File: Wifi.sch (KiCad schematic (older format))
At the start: 15 parts

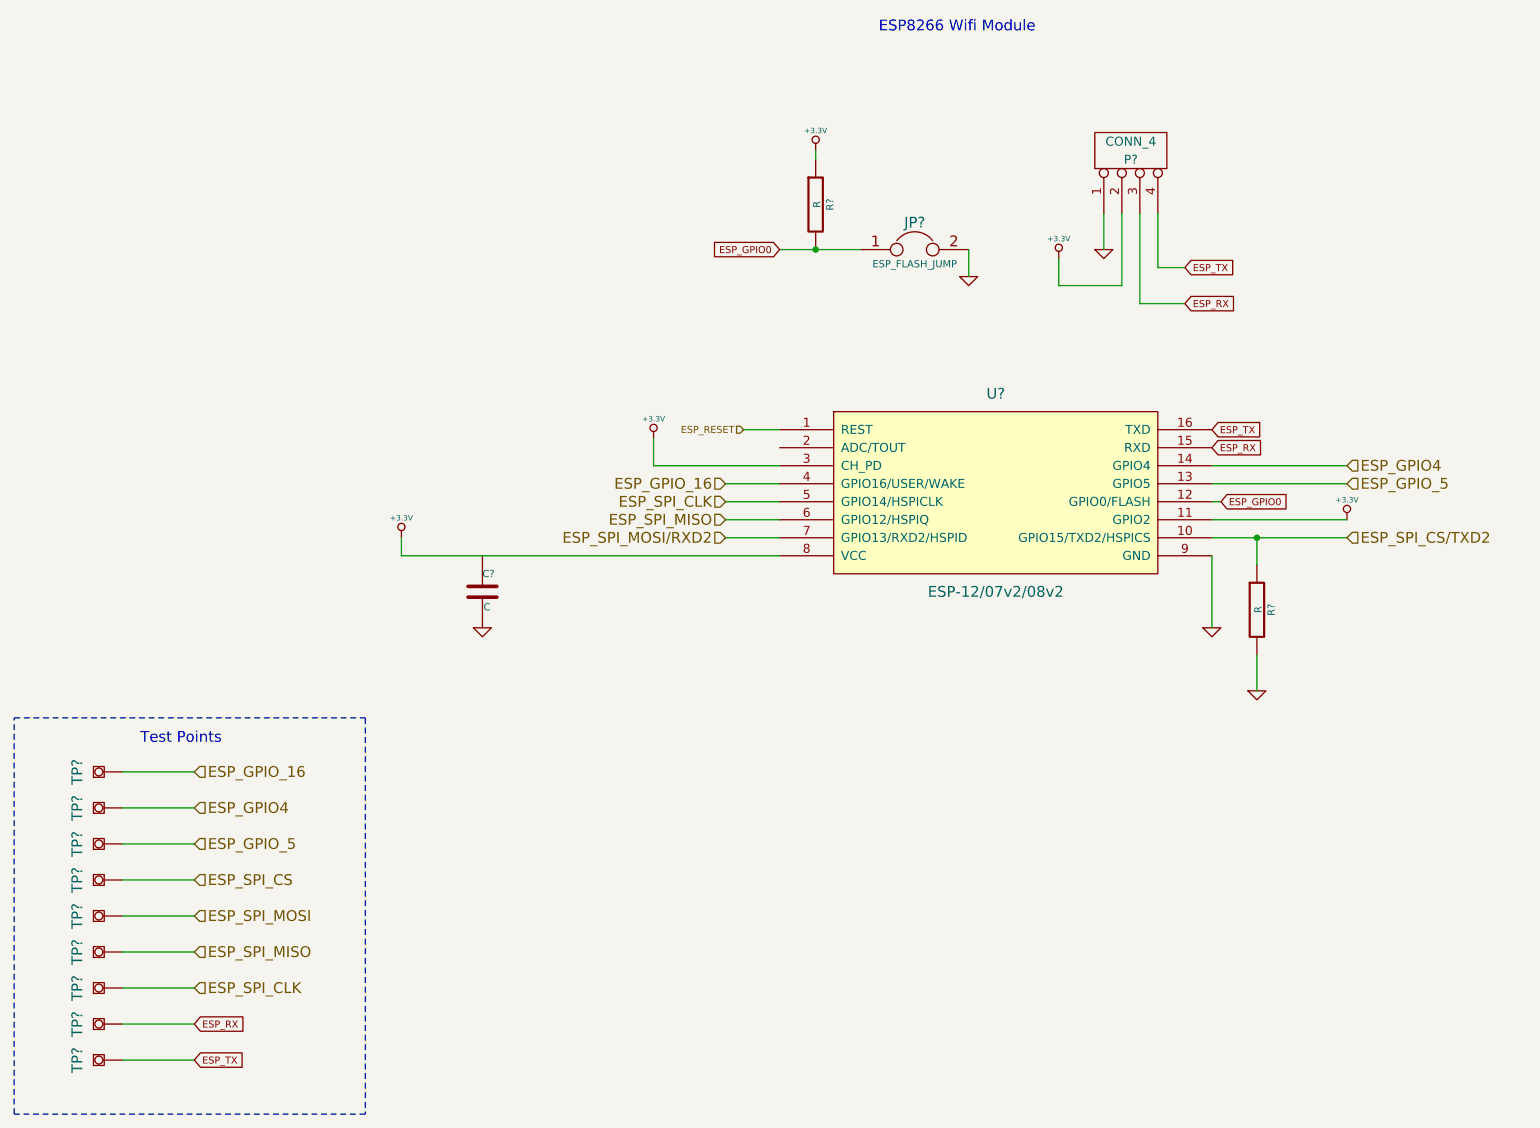
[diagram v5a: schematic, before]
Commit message: ESP doesn't seem to support UART2, switch to UART1
As far as I can tell the TXD2, RXD2 ports are not documented
If they do work, they will only work exclusively of TX1/RX1.
So better to just use the main UART.
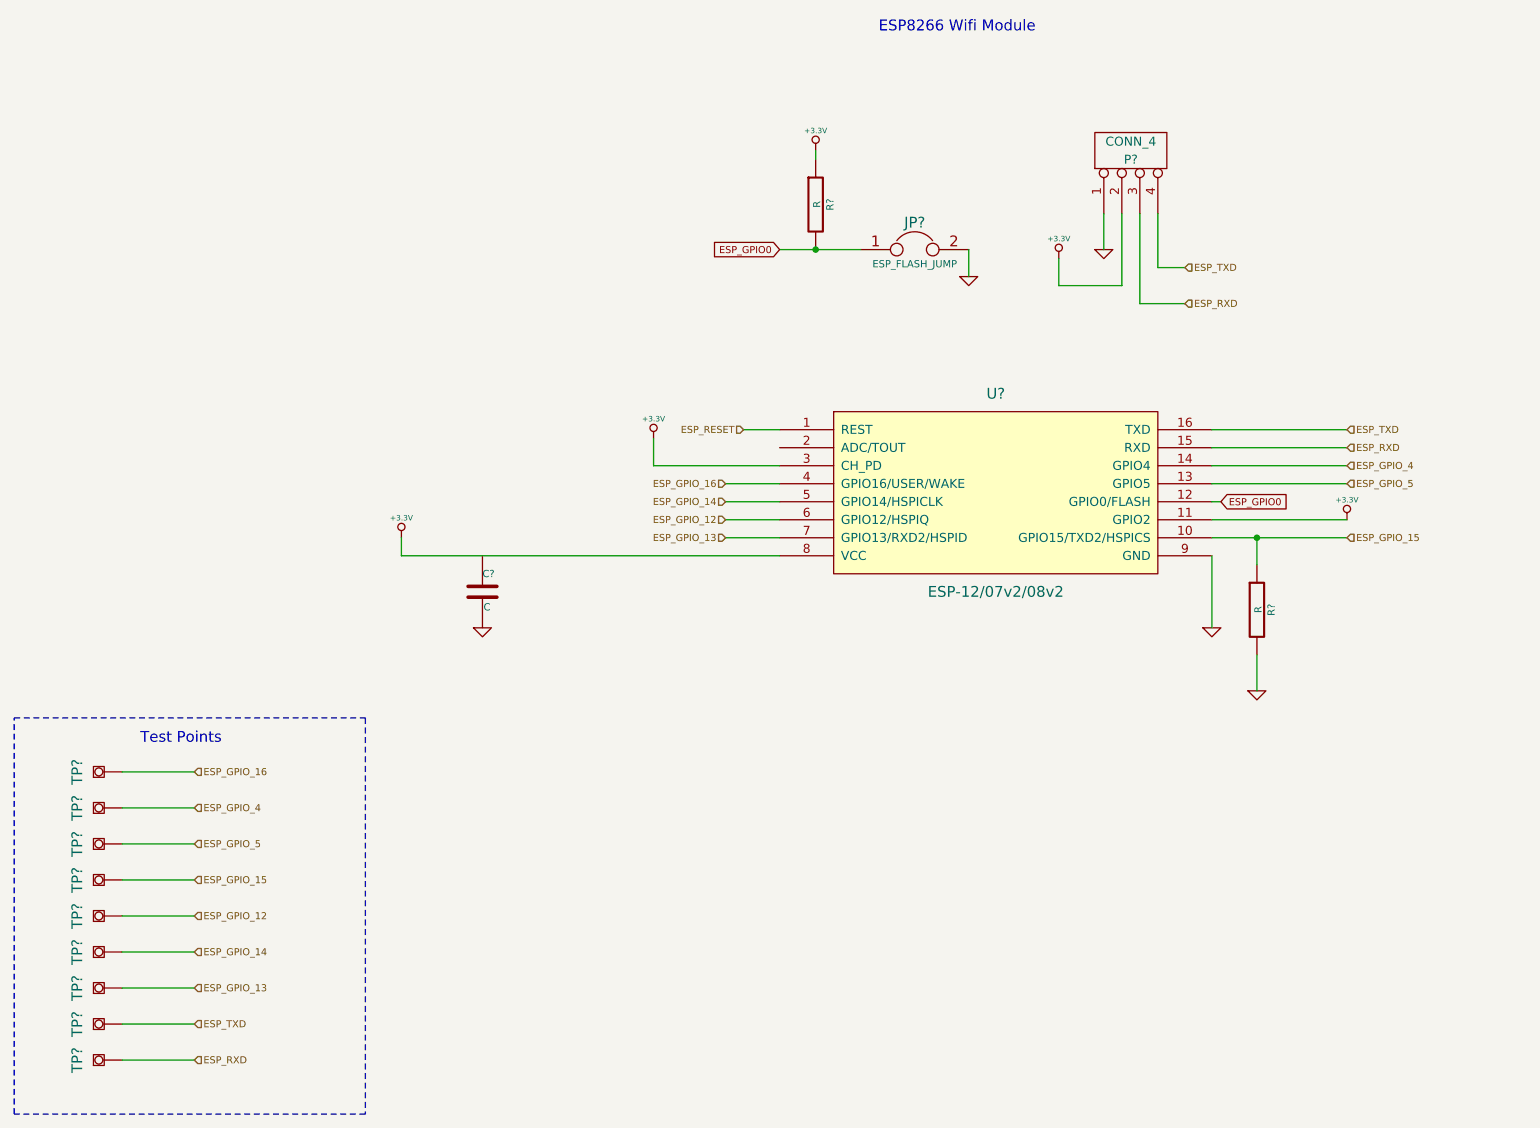
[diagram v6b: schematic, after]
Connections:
- net ESP_SPI_CS/TXD2 is gone; now on net ESP_GPIO_15: R?.1, U?.10 (GPIO15/TXD2/HSPICS)
- net ESP_SPI_MOSI is gone; now on net ESP_GPIO_12: TP?.1
- net ESP_SPI_MOSI/RXD2 is gone; now on net ESP_GPIO_13: U?.7 (GPIO13/RXD2/HSPID)
- net ESP_GPIO4 renamed ESP_GPIO_4
- net ESP_RX renamed ESP_RXD
- net ESP_RXD: now also TP?.1; no longer TP?.1
- net ESP_SPI_CLK renamed ESP_GPIO_13
- net ESP_GPIO_13: no longer U?.5 (GPIO14/HSPICLK)
- net ESP_SPI_CS renamed ESP_GPIO_15
- net ESP_SPI_MISO renamed ESP_GPIO_12
- net ESP_GPIO_12: no longer TP?.1
- net ESP_TX renamed ESP_TXD
- net ESP_TXD: now also TP?.1; no longer TP?.1
- new net ESP_GPIO_14: TP?.1, U?.5 (GPIO14/HSPICLK)
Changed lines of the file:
@@
 	1    0    0    -1
 $EndComp
-Text GLabel 7100 3200 2    39   Input ~ 0
-ESP_RX
-Text GLabel 7100 3000 2    39   Input ~ 0
-ESP_TX
 $Comp
 L JUMPER JP?
@@
 	1    0    0    -1
 $EndComp
-Text GLabel 7250 4000 2    39   Input ~ 0
-ESP_RX
-Text GLabel 1600 7400 2    39   Input ~ 0
-ESP_TX
-Text HLabel 4550 4300 0    60   Input ~ 0
-ESP_SPI_CLK
-Text HLabel 4550 4400 0    60   Input ~ 0
-ESP_SPI_MISO
-Text HLabel 4550 4500 0    60   Input ~ 0
-ESP_SPI_MOSI/RXD2
 $Comp
 L R R?
@@
 	1    0    0    -1
 $EndComp
-Text HLabel 8000 4500 2    60   Input ~ 0
-ESP_SPI_CS/TXD2
 $Comp
 L +3.3V #PWR?
@@
 Text GLabel 7300 4300 2    39   Input ~ 0
 ESP_GPIO0
-Text HLabel 8000 4100 2    60   Input ~ 0
-ESP_GPIO4
-Text HLabel 8000 4200 2    60   Input ~ 0
+Text HLabel 8000 4100 2    39   Input ~ 0
+ESP_GPIO_4
+Text HLabel 8000 4200 2    39   Input ~ 0
 ESP_GPIO_5
-Text HLabel 4550 4200 0    60   Input ~ 0
+Text HLabel 4550 4200 0    39   Input ~ 0
 ESP_GPIO_16
 $Comp
@@
 Wire Wire Line
 	1200 7000 1600 7000
-Text HLabel 1600 5800 2    60   Input ~ 0
+Text HLabel 1600 5800 2    39   Input ~ 0
 ESP_GPIO_16
-Text HLabel 1600 7000 2    60   Input ~ 0
-ESP_SPI_CLK
-Text HLabel 1600 6800 2    60   Input ~ 0
-ESP_SPI_MISO
-Text HLabel 1600 6600 2    60   Input ~ 0
-ESP_SPI_MOSI
-Text HLabel 1600 6400 2    60   Input ~ 0
-ESP_SPI_CS
-Text HLabel 1600 6200 2    60   Input ~ 0
+Text HLabel 1600 6200 2    39   Input ~ 0
 ESP_GPIO_5
-Text HLabel 1600 6000 2    60   Input ~ 0
-ESP_GPIO4
+Text HLabel 1600 6000 2    39   Input ~ 0
+ESP_GPIO_4
 $Comp
 L TESTPOINT TP?
@@
 Wire Wire Line
 	1200 7400 1600 7400
-Text GLabel 1600 7200 2    39   Input ~ 0
-ESP_RX
-Text GLabel 7250 3900 2    39   Input ~ 0
-ESP_TX
 Wire Notes Line
 	600  5500 2550 5500
@@
 Text HLabel 4650 3900 0    39   Input ~ 0
 ESP_RESET
+Text HLabel 8000 3900 2    39   Input ~ 0
+ESP_TXD
+Text HLabel 8000 4000 2    39   Input ~ 0
+ESP_RXD
+Text HLabel 7100 3200 2    39   Input ~ 0
+ESP_RXD
+Text HLabel 7100 3000 2    39   Input ~ 0
+ESP_TXD
+Wire Wire Line
+	8000 4000 7250 4000
+Wire Wire Line
+	7250 3900 8000 3900
+Text HLabel 1600 7200 2    39   Input ~ 0
+ESP_TXD
+Text HLabel 1600 7400 2    39   Input ~ 0
+ESP_RXD
+Text HLabel 4550 4300 0    39   Input ~ 0
+ESP_GPIO_14
+Text HLabel 4550 4400 0    39   Input ~ 0
+ESP_GPIO_12
+Text HLabel 4550 4500 0    39   Input ~ 0
+ESP_GPIO_13
+Text HLabel 8000 4500 2    39   Input ~ 0
+ESP_GPIO_15
+Text HLabel 1600 6400 2    39   Input ~ 0
+ESP_GPIO_15
+Text HLabel 1600 6600 2    39   Input ~ 0
+ESP_GPIO_12
+Text HLabel 1600 6800 2    39   Input ~ 0
+ESP_GPIO_14
+Text HLabel 1600 7000 2    39   Input ~ 0
+ESP_GPIO_13
 $EndSCHEMATC

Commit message: Think sch finished
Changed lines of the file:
@@
 $EndComp
 $Comp
-L GND #PWR?
+L GND #PWR054
 U 1 1 55667722
 P 6650 2900
-F 0 "#PWR?" H 6650 2900 30  0001 C CNN
+F 0 "#PWR054" H 6650 2900 30  0001 C CNN
 F 1 "GND" H 6650 2830 30  0001 C CNN
 F 2 "" H 6650 2900 60  0000 C CNN
@@
 $EndComp
 $Comp
-L +3.3V #PWR?
+L +3.3V #PWR055
 U 1 1 55667729
 P 6400 2950
-F 0 "#PWR?" H 6400 2910 30  0001 C CNN
+F 0 "#PWR055" H 6400 2910 30  0001 C CNN
 F 1 "+3.3V" H 6400 3060 30  0000 C CNN
 F 2 "" H 6400 2950 60  0000 C CNN
@@
 $EndComp
 $Comp
-L +3.3V #PWR?
+L +3.3V #PWR056
 U 1 1 55667746
 P 5050 2350
-F 0 "#PWR?" H 5050 2310 30  0001 C CNN
+F 0 "#PWR056" H 5050 2310 30  0001 C CNN
 F 1 "+3.3V" H 5050 2460 30  0000 C CNN
 F 2 "" H 5050 2350 60  0000 C CNN
@@
 $EndComp
 $Comp
-L GND #PWR?
+L GND #PWR057
 U 1 1 5566774C
 P 5900 3050
-F 0 "#PWR?" H 5900 3050 30  0001 C CNN
+F 0 "#PWR057" H 5900 3050 30  0001 C CNN
 F 1 "GND" H 5900 2980 30  0001 C CNN
 F 2 "" H 5900 3050 60  0000 C CNN
@@
 ESP8266 Wifi Module
 $Comp
-L +3.3V #PWR?
+L +3.3V #PWR058
 U 1 1 5566775A
 P 8000 4400
-F 0 "#PWR?" H 8000 4360 30  0001 C CNN
+F 0 "#PWR058" H 8000 4360 30  0001 C CNN
 F 1 "+3.3V" H 8000 4510 30  0000 C CNN
 F 2 "" H 8000 4400 60  0000 C CNN
@@
 $EndComp
 $Comp
-L +3.3V #PWR?
+L +3.3V #PWR059
 U 1 1 55667760
 P 4150 3950
-F 0 "#PWR?" H 4150 3910 30  0001 C CNN
+F 0 "#PWR059" H 4150 3910 30  0001 C CNN
 F 1 "+3.3V" H 4150 4060 30  0000 C CNN
 F 2 "" H 4150 3950 60  0000 C CNN
@@
 $EndComp
 $Comp
-L GND #PWR?
+L GND #PWR060
 U 1 1 5566776E
 P 7500 5350
-F 0 "#PWR?" H 7500 5350 30  0001 C CNN
+F 0 "#PWR060" H 7500 5350 30  0001 C CNN
 F 1 "GND" H 7500 5280 30  0001 C CNN
 F 2 "" H 7500 5350 60  0000 C CNN
@@
 $EndComp
 $Comp
-L +3.3V #PWR?
+L +3.3V #PWR061
 U 1 1 5566915C
 P 2750 4500
-F 0 "#PWR?" H 2750 4460 30  0001 C CNN
+F 0 "#PWR061" H 2750 4460 30  0001 C CNN
 F 1 "+3.3V" H 2750 4610 30  0000 C CNN
 F 2 "" H 2750 4500 60  0000 C CNN
@@
 $EndComp
 $Comp
-L GND #PWR?
+L GND #PWR062
 U 1 1 556691BF
 P 7250 5000
-F 0 "#PWR?" H 7250 5000 30  0001 C CNN
+F 0 "#PWR062" H 7250 5000 30  0001 C CNN
 F 1 "GND" H 7250 4930 30  0001 C CNN
 F 2 "" H 7250 5000 60  0000 C CNN
@@
 $EndComp
 $Comp
-L GND #PWR?
+L GND #PWR063
 U 1 1 5566925F
 P 3200 5000
-F 0 "#PWR?" H 3200 5000 30  0001 C CNN
+F 0 "#PWR063" H 3200 5000 30  0001 C CNN
 F 1 "GND" H 3200 4930 30  0001 C CNN
 F 2 "" H 3200 5000 60  0000 C CNN
@@
 	5050 2350 5050 2400
 Wire Wire Line
-	4850 2900 5300 2900
+	4850 2900 5050 2900
+Wire Wire Line
+	5050 2900 5300 2900
 Wire Wire Line
 	5900 2900 5900 3050
@@
 	7250 4300 7300 4300
 Wire Wire Line
-	7250 4500 8000 4500
+	7250 4500 7500 4500
+Wire Wire Line
+	7500 4500 8000 4500
 Wire Wire Line
 	7500 4500 7500 4650
@@
 Text HLabel 7100 3000 2    39   Input ~ 0
 ESP_TXD
-Wire Wire Line
-	8000 4000 7250 4000
-Wire Wire Line
-	7250 3900 8000 3900
 Text HLabel 1600 7200 2    39   Input ~ 0
 ESP_TXD
@@
 Text HLabel 1600 7000 2    39   Input ~ 0
 ESP_GPIO_13
+Wire Wire Line
+	7250 3900 7950 3900
+Wire Wire Line
+	7950 3900 8000 3900
+Wire Wire Line
+	7250 4000 7650 4000
+Wire Wire Line
+	7650 4000 8000 4000
 $EndSCHEMATC

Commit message: DRCs mostly fixed
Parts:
- gave numbers to parts that had none: 15
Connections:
- net +3.3V: now also C12.1
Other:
- moved on the sheet: C12
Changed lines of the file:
@@
 $EndDescr
 $Comp
-L ESP-12/07v2/08v2 U?
+L ESP-12/07v2/08v2 U8
 U 1 1 55667714
 P 6050 4250
-F 0 "U?" H 6050 4800 60  0000 C CNN
+F 0 "U8" H 6050 4800 60  0000 C CNN
 F 1 "ESP-12/07v2/08v2" H 6050 3700 60  0000 C CNN
 F 2 "" H 6050 4250 60  0000 C CNN
@@
 $EndComp
 $Comp
-L CONN_4 P?
+L CONN_4 P5
 U 1 1 5566771B
 P 6800 2350
-F 0 "P?" V 6750 2350 50  0000 C CNN
+F 0 "P5" V 6750 2350 50  0000 C CNN
 F 1 "CONN_4" V 6850 2350 50  0000 C CNN
 F 2 "" H 6800 2350 60  0000 C CNN
@@
 $EndComp
 $Comp
-L GND #PWR054
+L GND #PWR056
 U 1 1 55667722
 P 6650 2900
-F 0 "#PWR054" H 6650 2900 30  0001 C CNN
+F 0 "#PWR056" H 6650 2900 30  0001 C CNN
 F 1 "GND" H 6650 2830 30  0001 C CNN
 F 2 "" H 6650 2900 60  0000 C CNN
@@
 $EndComp
 $Comp
-L +3.3V #PWR055
+L +3.3V #PWR057
 U 1 1 55667729
 P 6400 2950
-F 0 "#PWR055" H 6400 2910 30  0001 C CNN
+F 0 "#PWR057" H 6400 2910 30  0001 C CNN
 F 1 "+3.3V" H 6400 3060 30  0000 C CNN
 F 2 "" H 6400 2950 60  0000 C CNN
@@
 $EndComp
 $Comp
-L JUMPER JP?
+L JUMPER JP2
 U 1 1 55667738
 P 5600 2900
-F 0 "JP?" H 5600 3050 60  0000 C CNN
+F 0 "JP2" H 5600 3050 60  0000 C CNN
 F 1 "ESP_FLASH_JUMP" H 5600 2820 40  0000 C CNN
 F 2 "" H 5600 2900 60  0000 C CNN
@@
 $EndComp
 $Comp
-L R R?
+L R R10
 U 1 1 5566773F
 P 5050 2650
-F 0 "R?" V 5130 2650 40  0000 C CNN
+F 0 "R10" V 5130 2650 40  0000 C CNN
 F 1 "R" V 5057 2651 40  0000 C CNN
 F 2 "" V 4980 2650 30  0000 C CNN
@@
 $EndComp
 $Comp
-L +3.3V #PWR056
+L +3.3V #PWR058
 U 1 1 55667746
 P 5050 2350
-F 0 "#PWR056" H 5050 2310 30  0001 C CNN
+F 0 "#PWR058" H 5050 2310 30  0001 C CNN
 F 1 "+3.3V" H 5050 2460 30  0000 C CNN
 F 2 "" H 5050 2350 60  0000 C CNN
@@
 $EndComp
 $Comp
-L GND #PWR057
+L GND #PWR059
 U 1 1 5566774C
 P 5900 3050
-F 0 "#PWR057" H 5900 3050 30  0001 C CNN
+F 0 "#PWR059" H 5900 3050 30  0001 C CNN
 F 1 "GND" H 5900 2980 30  0001 C CNN
 F 2 "" H 5900 3050 60  0000 C CNN
@@
 ESP8266 Wifi Module
 $Comp
-L +3.3V #PWR058
+L +3.3V #PWR060
 U 1 1 5566775A
 P 8000 4400
-F 0 "#PWR058" H 8000 4360 30  0001 C CNN
+F 0 "#PWR060" H 8000 4360 30  0001 C CNN
 F 1 "+3.3V" H 8000 4510 30  0000 C CNN
 F 2 "" H 8000 4400 60  0000 C CNN
@@
 $EndComp
 $Comp
-L +3.3V #PWR059
+L +3.3V #PWR061
 U 1 1 55667760
 P 4150 3950
-F 0 "#PWR059" H 4150 3910 30  0001 C CNN
+F 0 "#PWR061" H 4150 3910 30  0001 C CNN
 F 1 "+3.3V" H 4150 4060 30  0000 C CNN
 F 2 "" H 4150 3950 60  0000 C CNN
@@
 $EndComp
 $Comp
-L GND #PWR060
+L GND #PWR062
 U 1 1 5566776E
 P 7500 5350
-F 0 "#PWR060" H 7500 5350 30  0001 C CNN
+F 0 "#PWR062" H 7500 5350 30  0001 C CNN
 F 1 "GND" H 7500 5280 30  0001 C CNN
 F 2 "" H 7500 5350 60  0000 C CNN
@@
 $EndComp
 $Comp
-L R R?
+L R R11
 U 1 1 55668FA2
 P 7500 4900
-F 0 "R?" V 7580 4900 40  0000 C CNN
+F 0 "R11" V 7580 4900 40  0000 C CNN
 F 1 "R" V 7507 4901 40  0000 C CNN
 F 2 "" V 7430 4900 30  0000 C CNN
@@
 $EndComp
 $Comp
-L +3.3V #PWR061
+L +3.3V #PWR063
 U 1 1 5566915C
 P 2750 4500
-F 0 "#PWR061" H 2750 4460 30  0001 C CNN
+F 0 "#PWR063" H 2750 4460 30  0001 C CNN
 F 1 "+3.3V" H 2750 4610 30  0000 C CNN
 F 2 "" H 2750 4500 60  0000 C CNN
@@
 $EndComp
 $Comp
-L GND #PWR062
+L GND #PWR064
 U 1 1 556691BF
 P 7250 5000
-F 0 "#PWR062" H 7250 5000 30  0001 C CNN
+F 0 "#PWR064" H 7250 5000 30  0001 C CNN
 F 1 "GND" H 7250 4930 30  0001 C CNN
 F 2 "" H 7250 5000 60  0000 C CNN
@@
 $EndComp
 $Comp
-L C C?
+L C C12
 U 1 1 5566923C
-P 3200 4800
-F 0 "C?" H 3200 4900 40  0000 L CNN
-F 1 "C" H 3206 4715 40  0000 L CNN
-F 2 "" H 3238 4650 30  0000 C CNN
-F 3 "" H 3200 4800 60  0000 C CNN
-	1    3200 4800
-	1    0    0    -1
-$EndComp
-$Comp
-L GND #PWR063
+P 3450 4850
+F 0 "C12" H 3450 4950 40  0000 L CNN
+F 1 "C" H 3456 4765 40  0000 L CNN
+F 2 "" H 3488 4700 30  0000 C CNN
+F 3 "" H 3450 4850 60  0000 C CNN
+	1    3450 4850
+	1    0    0    -1
+$EndComp
+$Comp
+L GND #PWR065
 U 1 1 5566925F
-P 3200 5000
-F 0 "#PWR063" H 3200 5000 30  0001 C CNN
-F 1 "GND" H 3200 4930 30  0001 C CNN
-F 2 "" H 3200 5000 60  0000 C CNN
-F 3 "" H 3200 5000 60  0000 C CNN
-	1    3200 5000
+P 3450 5150
+F 0 "#PWR065" H 3450 5150 30  0001 C CNN
+F 1 "GND" H 3450 5080 30  0001 C CNN
+F 2 "" H 3450 5150 60  0000 C CNN
+F 3 "" H 3450 5150 60  0000 C CNN
+	1    3450 5150
 	1    0    0    -1
 $EndComp
@@
 ESP_GPIO_16
 $Comp
-L TESTPOINT TP?
+L TESTPOINT TP2
 U 1 1 55669763
 P 1200 5800
-F 0 "TP?" H 1200 6050 60  0000 C CNN
+F 0 "TP2" H 1200 6050 60  0000 C CNN
 F 1 "TESTPOINT" H 1200 5750 60  0001 C CNN
 F 2 "" H 1200 5800 60  0000 C CNN
@@
 	5050 2350 5050 2400
 Wire Wire Line
-	4850 2900 5050 2900
-Wire Wire Line
-	5050 2900 5300 2900
+	4850 2900 5300 2900
 Wire Wire Line
 	5900 2900 5900 3050
@@
 	7250 4300 7300 4300
 Wire Wire Line
-	7250 4500 7500 4500
-Wire Wire Line
-	7500 4500 8000 4500
+	7250 4500 8000 4500
 Wire Wire Line
 	7500 4500 7500 4650
@@
 	4850 4500 4550 4500
 $Comp
-L TESTPOINT TP?
+L TESTPOINT TP3
 U 1 1 55669E4F
 P 1200 6000
-F 0 "TP?" H 1200 6250 60  0000 C CNN
+F 0 "TP3" H 1200 6250 60  0000 C CNN
 F 1 "TESTPOINT" H 1200 5950 60  0001 C CNN
 F 2 "" H 1200 6000 60  0000 C CNN
@@
 $EndComp
 $Comp
-L TESTPOINT TP?
+L TESTPOINT TP4
 U 1 1 55669E83
 P 1200 6200
-F 0 "TP?" H 1200 6450 60  0000 C CNN
+F 0 "TP4" H 1200 6450 60  0000 C CNN
 F 1 "TESTPOINT" H 1200 6150 60  0001 C CNN
 F 2 "" H 1200 6200 60  0000 C CNN
@@
 $EndComp
 $Comp
-L TESTPOINT TP?
+L TESTPOINT TP5
 U 1 1 55669EAD
 P 1200 6400
-F 0 "TP?" H 1200 6650 60  0000 C CNN
+F 0 "TP5" H 1200 6650 60  0000 C CNN
 F 1 "TESTPOINT" H 1200 6350 60  0001 C CNN
 F 2 "" H 1200 6400 60  0000 C CNN
@@
 $EndComp
 $Comp
-L TESTPOINT TP?
+L TESTPOINT TP6
 U 1 1 55669F01
 P 1200 6600
-F 0 "TP?" H 1200 6850 60  0000 C CNN
+F 0 "TP6" H 1200 6850 60  0000 C CNN
 F 1 "TESTPOINT" H 1200 6550 60  0001 C CNN
 F 2 "" H 1200 6600 60  0000 C CNN
@@
 $EndComp
 $Comp
-L TESTPOINT TP?
+L TESTPOINT TP7
 U 1 1 55669F33
 P 1200 6800
-F 0 "TP?" H 1200 7050 60  0000 C CNN
+F 0 "TP7" H 1200 7050 60  0000 C CNN
 F 1 "TESTPOINT" H 1200 6750 60  0001 C CNN
 F 2 "" H 1200 6800 60  0000 C CNN
@@
 $EndComp
 $Comp
-L TESTPOINT TP?
+L TESTPOINT TP8
 U 1 1 55669F6B
 P 1200 7000
-F 0 "TP?" H 1200 7250 60  0000 C CNN
+F 0 "TP8" H 1200 7250 60  0000 C CNN
 F 1 "TESTPOINT" H 1200 6950 60  0001 C CNN
 F 2 "" H 1200 7000 60  0000 C CNN
@@
 ESP_GPIO_4
 $Comp
-L TESTPOINT TP?
+L TESTPOINT TP9
 U 1 1 5566A6E7
 P 1200 7200
-F 0 "TP?" H 1200 7450 60  0000 C CNN
+F 0 "TP9" H 1200 7450 60  0000 C CNN
 F 1 "TESTPOINT" H 1200 7150 60  0001 C CNN
 F 2 "" H 1200 7200 60  0000 C CNN
@@
 	1200 7200 1600 7200
 $Comp
-L TESTPOINT TP?
+L TESTPOINT TP10
 U 1 1 5566A71B
 P 1200 7400
-F 0 "TP?" H 1200 7650 60  0000 C CNN
+F 0 "TP10" H 1200 7650 60  0000 C CNN
 F 1 "TESTPOINT" H 1200 7350 60  0001 C CNN
 F 2 "" H 1200 7400 60  0000 C CNN
@@
 ESP_GPIO_13
 Wire Wire Line
-	7250 3900 7950 3900
-Wire Wire Line
-	7950 3900 8000 3900
-Wire Wire Line
-	7250 4000 7650 4000
-Wire Wire Line
-	7650 4000 8000 4000
+	7250 3900 8000 3900
+Wire Wire Line
+	7250 4000 8000 4000
+Wire Wire Line
+	3450 4600 3450 4650
+Connection ~ 3450 4600
+Wire Wire Line
+	3450 5050 3450 5150
 $EndSCHEMATC
